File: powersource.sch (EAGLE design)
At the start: 6 parts

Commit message: fix
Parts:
- added B1: B1S, rectifier:B1S
- added C3: (no value), capacitor-wima:C10/5
- added TR1: (no value), inductor-neosid:U15-TRANSFORMER
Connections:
- new net N$2: B1.AC1, TR1.3
- new net N$3: B1.AC2, TR1.1
- new net V+: B1.+, B1.-, C3.1, C3.2
- new net VCC: TR1.4
- net GND: now also TR1.2
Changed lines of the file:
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@@
 <part name="R1" library="ngspice-simulation" library_urn="urn:adsk.eagle:library:527439" deviceset="R" device=""/>
 <part name="C2" library="capacitor-wima" library_urn="urn:adsk.eagle:library:116" deviceset="C" device="10/5" package3d_urn="urn:adsk.eagle:package:5399/1"/>
+<part name="B1" library="rectifier" library_urn="urn:adsk.eagle:library:336" deviceset="B*S" device="" package3d_urn="urn:adsk.eagle:package:23901/1" technology="1"/>
+<part name="TR1" library="inductor-neosid" library_urn="urn:adsk.eagle:library:241" deviceset="U15" device="-TRANSFORMER" package3d_urn="urn:adsk.eagle:package:14678/1"/>
+<part name="GND1" library="supply1" library_urn="urn:adsk.eagle:library:371" deviceset="GND" device=""/>
+<part name="P+1" library="supply1" library_urn="urn:adsk.eagle:library:371" deviceset="VCC" device="">
+<attribute name="AC100V" value=""/>
+</part>
+<part name="C3" library="capacitor-wima" library_urn="urn:adsk.eagle:library:116" deviceset="C" device="10/5" package3d_urn="urn:adsk.eagle:package:5399/1"/>
+<part name="SUPPLY2" library="supply2" library_urn="urn:adsk.eagle:library:372" deviceset="V+" device="">
+<attribute name="V-" value=""/>
+</part>
+<part name="SUPPLY3" library="supply2" library_urn="urn:adsk.eagle:library:372" deviceset="V+" device=""/>
 </parts>
 <sheets>
@@
 <attribute name="VALUE" x="-6.604" y="88.519" size="1.778" layer="96" rot="R180"/>
 </instance>
+<instance part="B1" gate="G$1" x="-27.94" y="116.84" smashed="yes">
+<attribute name="VALUE" x="-22.86" y="111.76" size="1.778" layer="96"/>
+<attribute name="NAME" x="-22.86" y="119.38" size="1.778" layer="95"/>
+</instance>
+<instance part="TR1" gate="G$1" x="-45.72" y="119.38" smashed="yes" rot="R180">
+<attribute name="NAME" x="-43.18" y="116.024" size="1.778" layer="95" rot="R180"/>
+<attribute name="VALUE" x="-42.926" y="124.46" size="1.778" layer="96" rot="R180"/>
+</instance>
+<instance part="GND1" gate="1" x="-53.34" y="106.68" smashed="yes">
+<attribute name="VALUE" x="-55.88" y="104.14" size="1.778" layer="96"/>
+</instance>
+<instance part="P+1" gate="VCC" x="-55.88" y="121.92" smashed="yes" rot="R90">
+<attribute name="VALUE" x="-53.34" y="119.38" size="1.778" layer="96" rot="R180"/>
+<attribute name="AC100V" x="-55.88" y="121.92" size="1.778" layer="96" rot="R90" display="name"/>
+</instance>
+<instance part="C3" gate="G$1" x="-15.24" y="111.76" smashed="yes" rot="R180">
+<attribute name="NAME" x="-16.764" y="111.379" size="1.778" layer="95" rot="R180"/>
+<attribute name="VALUE" x="-16.764" y="116.459" size="1.778" layer="96" rot="R180"/>
+</instance>
+<instance part="SUPPLY2" gate="1" x="-7.62" y="109.22" smashed="yes" rot="R270">
+<attribute name="V-" x="-7.62" y="109.22" size="1.778" layer="96" rot="R270" display="name"/>
+</instance>
+<instance part="SUPPLY3" gate="1" x="-7.62" y="116.84" smashed="yes" rot="R270">
+<attribute name="VALUE" x="-6.35" y="118.11" size="1.778" layer="96" rot="R270"/>
+</instance>
 </instances>
 <busses>
@@
 <pinref part="GND11" gate="1" pin="GND"/>
 <pinref part="C1" gate="G$1" pin="1"/>
+</segment>
+<segment>
+<wire x1="-53.34" y1="116.84" x2="-53.34" y2="109.22" width="0.1524" layer="91"/>
+<pinref part="GND1" gate="1" pin="GND"/>
+<pinref part="TR1" gate="G$1" pin="2"/>
 </segment>
 </net>
@@
 </segment>
 </net>
+<net name="N$2" class="0">
+<segment>
+<pinref part="B1" gate="G$1" pin="AC1"/>
+<wire x1="-40.64" y1="121.92" x2="-27.94" y2="121.92" width="0.1524" layer="91"/>
+<pinref part="TR1" gate="G$1" pin="3"/>
+</segment>
+</net>
+<net name="N$3" class="0">
+<segment>
+<pinref part="B1" gate="G$1" pin="AC2"/>
+<wire x1="-40.64" y1="111.76" x2="-27.94" y2="111.76" width="0.1524" layer="91"/>
+<pinref part="TR1" gate="G$1" pin="1"/>
+<wire x1="-40.64" y1="116.84" x2="-40.64" y2="111.76" width="0.1524" layer="91"/>
+</segment>
+</net>
+<net name="VCC" class="0">
+<segment>
+<pinref part="TR1" gate="G$1" pin="4"/>
+<pinref part="P+1" gate="VCC" pin="VCC"/>
+</segment>
+</net>
+<net name="V+" class="0">
+<segment>
+<pinref part="B1" gate="G$1" pin="-"/>
+<wire x1="-33.02" y1="116.84" x2="-33.02" y2="109.22" width="0.1524" layer="91"/>
+<wire x1="-33.02" y1="109.22" x2="-15.24" y2="109.22" width="0.1524" layer="91"/>
+<pinref part="C3" gate="G$1" pin="1"/>
+<wire x1="-10.16" y1="109.22" x2="-15.24" y2="109.22" width="0.1524" layer="91"/>
+<junction x="-15.24" y="109.22"/>
+<pinref part="SUPPLY2" gate="1" pin="V+"/>
+</segment>
+<segment>
+<pinref part="B1" gate="G$1" pin="+"/>
+<wire x1="-22.86" y1="116.84" x2="-15.24" y2="116.84" width="0.1524" layer="91"/>
+<pinref part="C3" gate="G$1" pin="2"/>
+<wire x1="-15.24" y1="116.84" x2="-10.16" y2="116.84" width="0.1524" layer="91"/>
+<junction x="-15.24" y="116.84"/>
+<pinref part="SUPPLY3" gate="1" pin="V+"/>
+</segment>
+</net>

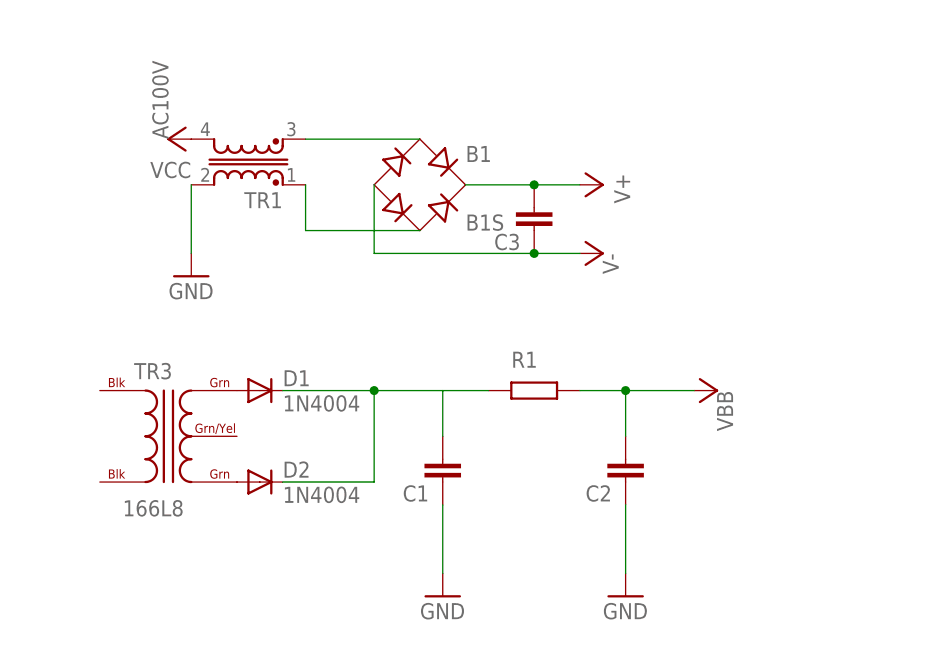
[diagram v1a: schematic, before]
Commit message: [add]電源の基板
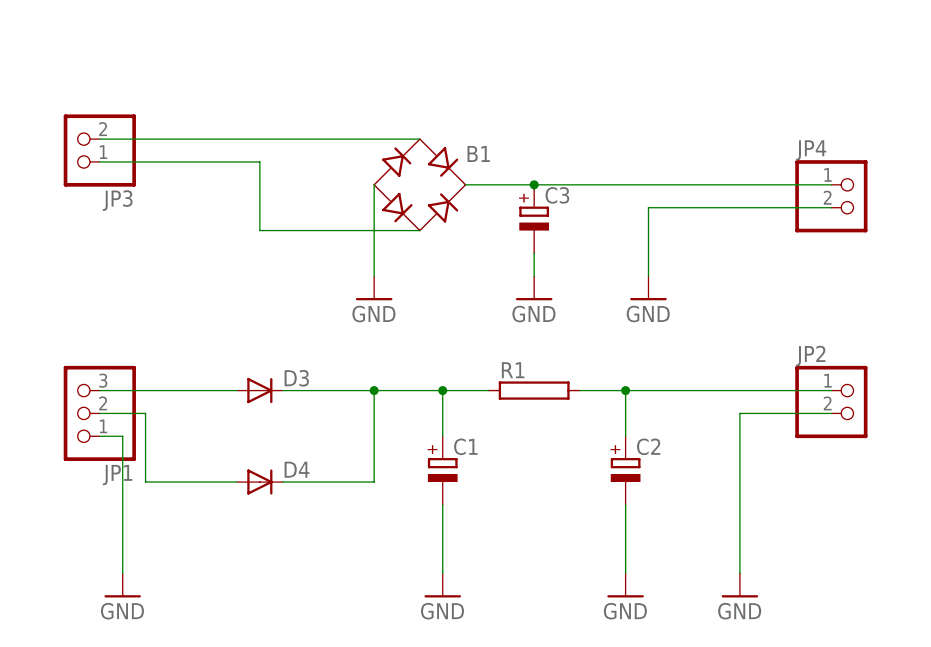
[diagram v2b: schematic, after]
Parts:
- removed D1, D2: 1N4004, diode:1N4004
- removed TR1: (no value), inductor-neosid:U15-TRANSFORMER
- removed TR3: 166L8, trafo-hammondmfg:166L8
- added D3, D4: (no value), diode:DIODE-DO07
- added JP1: (no value), pinhead:PINHD-1X3
- added JP2, JP3, JP4: (no value), pinhead:PINHD-1X2
- C1: device capacitor-wima:C10/5 -> rcl:CPOL-EUE7.5-16
- C2, C3: device capacitor-wima:C10/5 -> rcl:CPOL-EUE7.5-18
- R1: device ngspice-simulation:R -> resistor-power:RRWM10X65
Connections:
- removed net N$1: R1.1
- removed net N$13: D1.A, TR3.GRN@1
- removed net N$16: D2.A, TR3.GRN@2
- removed net V+: B1.+, B1.-, C3.1, C3.2
- removed net VCC: TR1.4
- new net N$4: B1.AC2, JP3.1
- new net N$5: B1.AC1, JP3.2
- new net N$7: B1.+, C3.+, JP4.1
- net GND: now also B1.-, C1.-, C2.-, C3.-, JP1.1, JP2.2, JP4.2; no longer C1.1, C2.1, TR1.2
- net N$14: now also C2.+, JP2.1; no longer C2.2
- net N$15: now also C1.+, D3.C, D4.C, R1.1; no longer C1.2, D1.C, D2.C
- net N$2: now also D3.A, JP1.3; no longer B1.AC1, TR1.3
- net N$3: now also D4.A, JP1.2; no longer B1.AC2, TR1.1

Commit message: [add]電源回路をいい感じにした
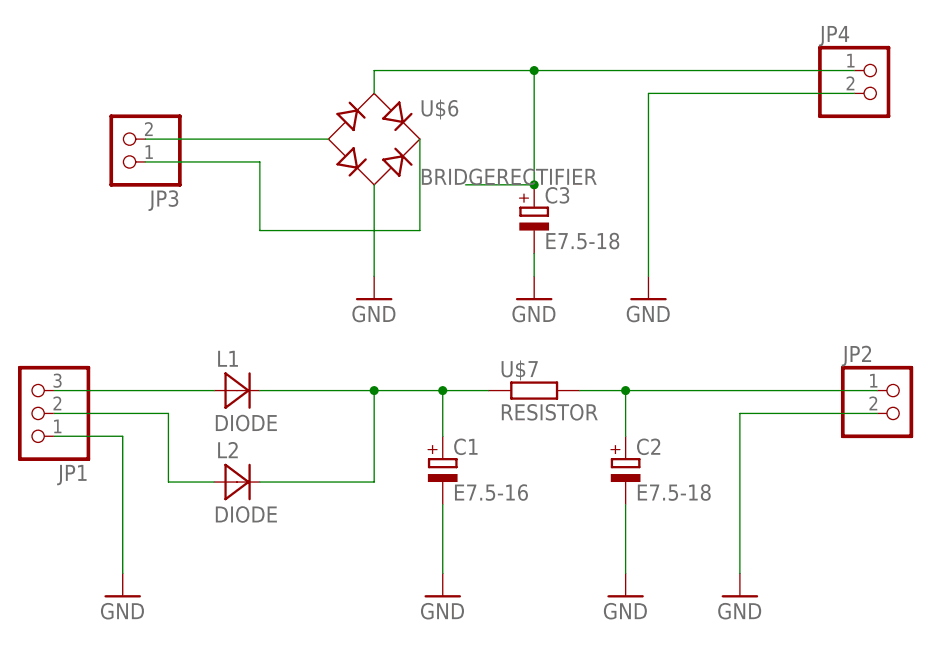
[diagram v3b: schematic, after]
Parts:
- removed B1: B1S, rectifier:B1S
- removed D3, D4: (no value), diode:DIODE-DO07
- removed R1: (no value), resistor-power:RRWM10X65
- added L1, L2: DIODE, VacuumTube:DIODE
- added U$6: BRIDGERECTIFIER, VacuumTube:BRIDGERECTIFIER
- added U$7: RESISTOR, VacuumTube:RESISTOR
- C1: value (none) -> E7.5-16; device rcl:CPOL-EUE7.5-16 -> VacuumTube:E7.5-16
- C2, C3: value (none) -> E7.5-18; device rcl:CPOL-EUE7.5-18 -> VacuumTube:E7.5-18
- JP1: device pinhead:PINHD-1X3 -> VacuumTube:PINHD-1X3
- JP2, JP3, JP4: device pinhead:PINHD-1X2 -> VacuumTube:PINHD-1X2
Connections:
- removed net N$5: B1.AC1, JP3.2
- new net N$1: JP1.2, L2.A
- net GND: now also U$6.AC2; no longer B1.-
- net N$14: now also U$7.2; no longer R1.2
- net N$15: now also L1.C, L2.C, U$7.1; no longer D3.C, D4.C, R1.1
- net N$2: now also L1.A; no longer D3.A
- net N$3: now also JP3.2, U$6.-; no longer D4.A, JP1.2
- net N$4: now also U$6.+; no longer B1.AC2
- net N$7: now also U$6.AC1; no longer B1.+
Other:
- moved on the sheet: JP1, JP2, JP3, JP4
